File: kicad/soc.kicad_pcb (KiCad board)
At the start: 2 copper layers, 0 parts

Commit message: some kicad stuff
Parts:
- added C1: .001uF, Capacitors_SMD:C_0603_HandSoldering, F.Cu at (78.7, 86.4)
- added J1: JACK_TRS_3PINS, mstock-pretty:SJI-3513N, F.Cu at (134.6, 111.8)
- added J2: PS/2 Keyboard, mstock-pretty:MD-60S, F.Cu at (130.8, 96.5)
- added J3: PS/2 Mouse, mstock-pretty:MD-60S, F.Cu at (130.8, 81.3)
- added P1: LED MATRIX, Pin_Headers:Pin_Header_Straight_2x08, F.Cu at (61.0, 77.5)
- added P10: CODEC right, Socket_Strips:Socket_Strip_Straight_1x16, F.Cu at (148.6, 67.3)
- added P11: CODEC inputs, Pin_Headers:Pin_Header_Straight_1x04, F.Cu at (167.6, 52.1)
- added P2: ALTERA_DE1_GPIO, mstock:PIN_ARRAY_20X2_LARGE, F.Cu at (52.1, 99.1)
- added P3: RTC header, Socket_Strips:Socket_Strip_Straight_1x07, F.Cu at (95.2, 92.7)
- added P6: Amp in, Socket_Strips:Socket_Strip_Straight_1x02, F.Cu at (96.5, 102.9)
- added P7: Amp pwr, Socket_Strips:Socket_Strip_Straight_1x03, F.Cu at (78.7, 116.8)
- added P8: Amp out, Socket_Strips:Socket_Strip_Straight_1x02, F.Cu at (78.7, 102.9)
- added P9: CODEC left, Socket_Strips:Socket_Strip_Straight_1x16, F.Cu at (105.4, 143.5)
- added R1: 10k, Resistors_SMD:R_0603_HandSoldering, F.Cu at (73.7, 86.4)
- added R2: 10k, Resistors_SMD:R_0603_HandSoldering, F.Cu at (83.8, 86.4)
- added R3: 10k, Resistors_SMD:R_0603_HandSoldering, F.Cu at (73.7, 104.1)
- added SP1: SPEAKER, Pin_Headers:Pin_Header_Angled_1x02, F.Cu at (86.4, 77.5)
- added U1: speakjet, Housings_DIP:DIP-18_W7.62mm, F.Cu at (61.0, 87.6)

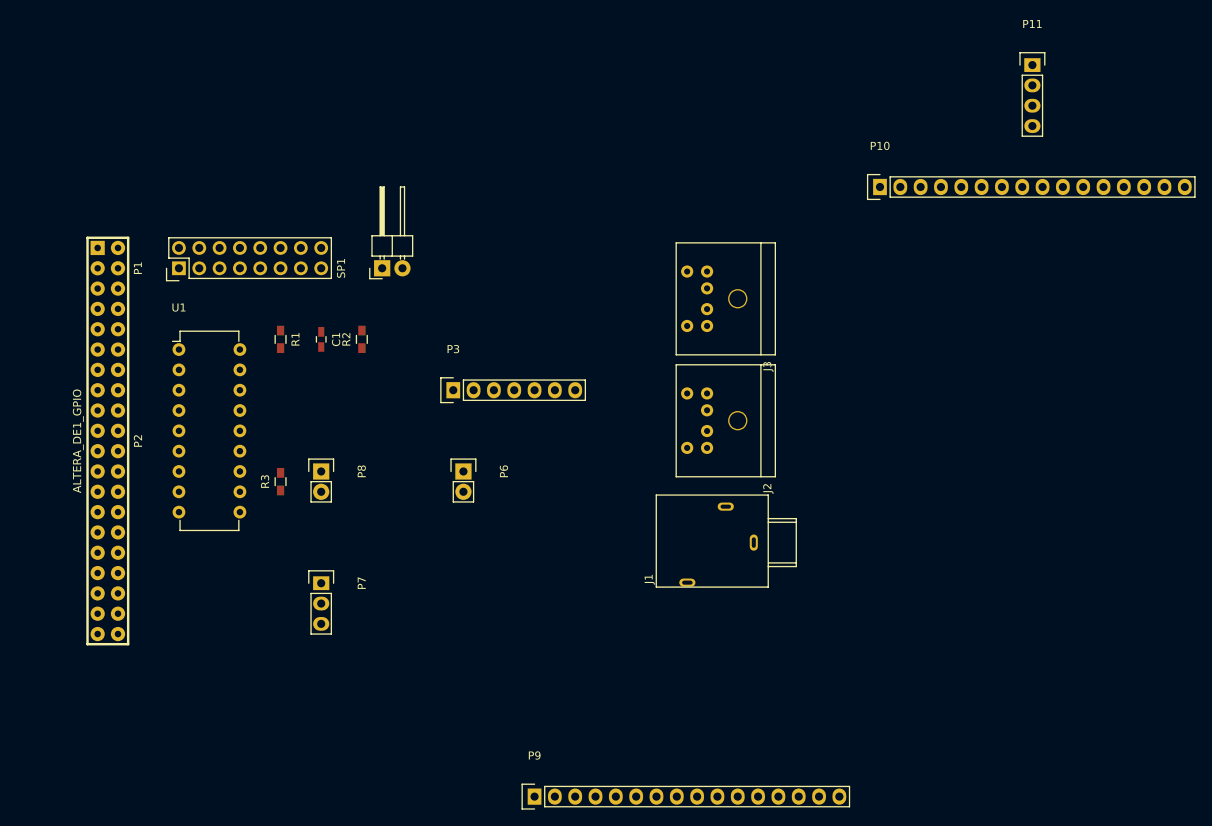
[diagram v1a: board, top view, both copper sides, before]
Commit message: some rework of support board, using the CODEC carrier board, the RTC, and headphone, PS/2 jacks
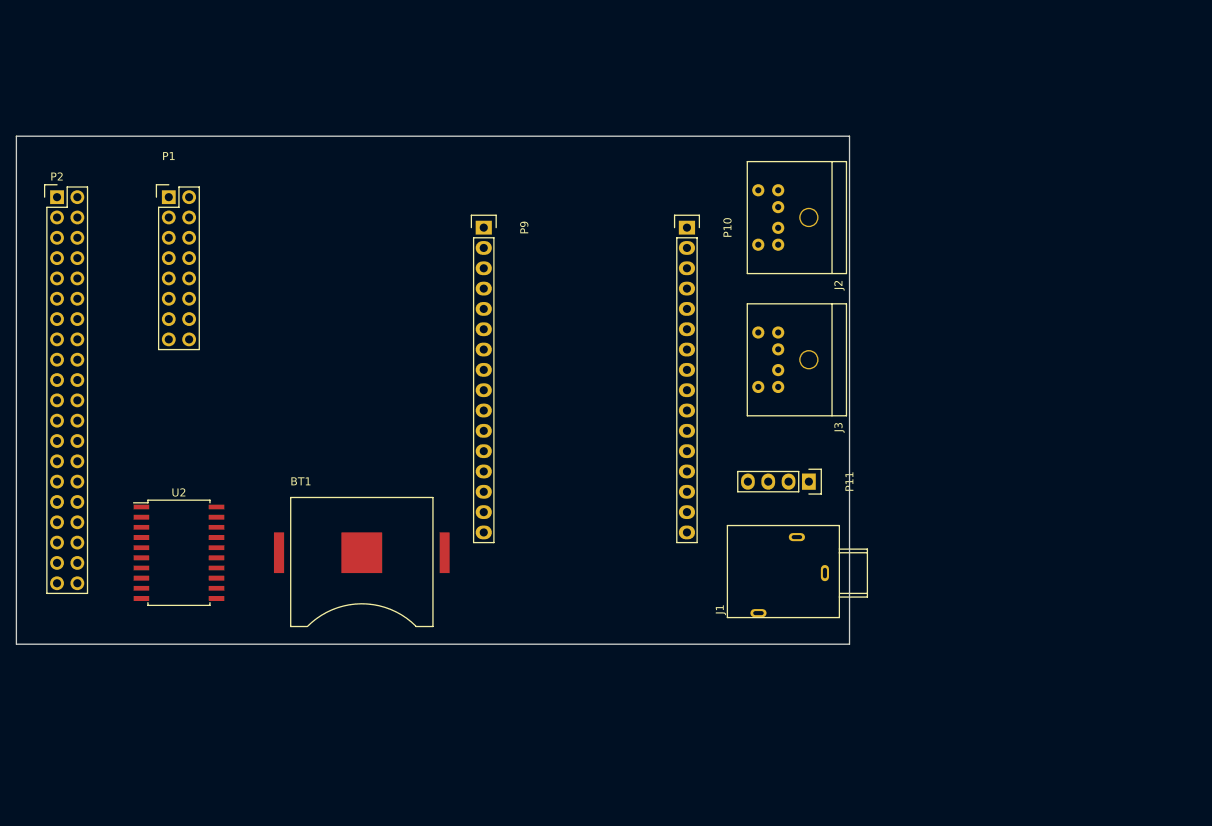
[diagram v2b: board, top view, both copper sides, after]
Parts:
- removed C1: .001uF, Capacitors_SMD:C_0603_HandSoldering
- removed P3: RTC header, Socket_Strips:Socket_Strip_Straight_1x07
- removed P6: Amp in, Socket_Strips:Socket_Strip_Straight_1x02
- removed P7: Amp pwr, Socket_Strips:Socket_Strip_Straight_1x03
- removed P8: Amp out, Socket_Strips:Socket_Strip_Straight_1x02
- removed R1, R2, R3: 10k, Resistors_SMD:R_0603_HandSoldering
- removed SP1: SPEAKER, Pin_Headers:Pin_Header_Angled_1x02
- removed U1: speakjet, Housings_DIP:DIP-18_W7.62mm
- added BT1: 2025 coin cell, mstock-pretty:coincell, F.Cu at (83.8, 113.0)
- added U2: DS3234, Housings_SOIC:SOIC-20_7.5x12.8mm_Pitch1.27mm, F.Cu at (61.0, 113.0)
- P2: footprint mstock:PIN_ARRAY_20X2_LARGE -> Pin_Headers:Pin_Header_Straight_2x20
- moved P9 71.4 mm to (99.1, 72.4), turned to 270 degrees
- moved P11 59.1 mm to (139.7, 104.1), turned to 270 degrees
- moved P2 31.1 mm to (45.7, 68.6), turned to 0 degrees
- moved J2 26.9 mm to (139.7, 71.1)
- moved P10 24.7 mm to (124.5, 72.4), turned to 270 degrees
- moved J3 11.7 mm to (139.7, 88.9)
- moved J1 9.67 mm to (143.5, 115.6)
- moved P1 8.98 mm to (59.7, 68.6), turned to 0 degrees
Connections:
- P2 pad 1: /Serial1 -> (no net)
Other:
- board outline added: 104.1 x 63.5 mm

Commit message: close to final
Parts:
- removed P11: CODEC inputs, Pin_Headers:Pin_Header_Straight_1x04
- added C1: 10nF, Capacitors_SMD:C_0805_HandSoldering, F.Cu at (106.7, 100.3)
- added C2: 10nF, Capacitors_SMD:C_0805_HandSoldering, F.Cu at (106.7, 92.7)
- added C3: 1uF, Capacitors_SMD:C_0805_HandSoldering, F.Cu at (114.3, 100.3)
- added C4: 1uF, Capacitors_SMD:C_0805_HandSoldering, F.Cu at (114.3, 92.7)
- added J4: Line In, mstock-pretty:SJI-3513N, F.Cu at (143.5, 102.9)
- added P3: Bluetooth, Socket_Strips:Socket_Strip_Straight_1x09, F.Cu at (71.1, 85.1)
- added P4: CONN_01X08, Pin_Headers:Pin_Header_Straight_2x04, F.Cu at (57.1, 92.7)
- added R1: 470, Resistors_SMD:R_0805_HandSoldering, F.Cu at (114.3, 106.7)
- added R2: 470, Resistors_SMD:R_0805_HandSoldering, F.Cu at (114.3, 86.4)
- J1: value JACK_TRS_3PINS -> Line Out
- moved P1 3.59 mm to (57.1, 66.0)
- moved BT1 2.54 mm to (81.3, 113.0)
- moved J1 1.27 mm to (143.5, 116.8)
- moved J2 1.27 mm to (139.7, 69.8)
- moved J3 1.27 mm to (139.7, 87.6)
- moved U2 1.27 mm to (59.7, 113.0)
- moved P10 1.27 mm to (123.2, 72.4)
- moved P9 1.27 mm to (100.3, 72.4)
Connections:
- net Net-(J1-Pad2) renamed /L_OUT
- net Net-(J1-Pad3) renamed /R_OUT
- J1 pad 1: Net-(J1-Pad1) -> GNDA
- J2 pad 2: (no net) -> Net-(J2-Pad2)
- J2 pad 6: (no net) -> Net-(J2-Pad6)
- J3 pad 2: (no net) -> Net-(J3-Pad2)
- J3 pad 6: (no net) -> Net-(J3-Pad6)
- P1 pad 12: (no net) -> Net-(P1-Pad12)
- P10 pad 1: (no net) -> Net-(P10-Pad1)
- P10 pad 10: (no net) -> Net-(P10-Pad10)
- P10 pad 11: (no net) -> Net-(P10-Pad11)
- P10 pad 12: (no net) -> Net-(P10-Pad12)
- P10 pad 13: Net-(P10-Pad13) -> GNDA
- P10 pad 15: Net-(P10-Pad15) -> /L_IN
- P10 pad 16: Net-(P10-Pad16) -> /R_IN
- P10 pad 2: (no net) -> Net-(P10-Pad2)
- P10 pad 3: (no net) -> Net-(P10-Pad3)
- P10 pad 4: (no net) -> Net-(P10-Pad4)
- P10 pad 5: (no net) -> Net-(P10-Pad5)
- P10 pad 6: (no net) -> Net-(P10-Pad6)
- P10 pad 7: (no net) -> Net-(P10-Pad7)
- P10 pad 8: (no net) -> Net-(P10-Pad8)
- P10 pad 9: (no net) -> Net-(P10-Pad9)
- P2 pad 1: (no net) -> /Serial1
- P2 pad 20: (no net) -> /IO_17
- P2 pad 21: (no net) -> /~BLE_CS
- P2 pad 22: (no net) -> /IO_19
- P2 pad 23: (no net) -> /IO_20
- P2 pad 24: (no net) -> /BLE_IRQ
- P2 pad 35: (no net) -> /IO_30
- P2 pad 36: (no net) -> /IO_31
- P2 pad 37: (no net) -> /IO_32
- P9 pad 13: Net-(J1-Pad1) -> GNDA
- P9 pad 14: Net-(J1-Pad1) -> GNDA
- P9 pad 2: (no net) -> Net-(P9-Pad2)
- P9 pad 9: (no net) -> Net-(P9-Pad9)
- U2 pad 10: (no net) -> Net-(U2-Pad10)
- U2 pad 11: (no net) -> Net-(U2-Pad11)
- U2 pad 12: (no net) -> Net-(U2-Pad12)
- U2 pad 13: (no net) -> Net-(U2-Pad13)
- U2 pad 14: (no net) -> Net-(U2-Pad14)
- U2 pad 2: (no net) -> Net-(U2-Pad2)
- U2 pad 3: (no net) -> Net-(U2-Pad3)
- U2 pad 5: (no net) -> Net-(U2-Pad5)
- U2 pad 6: (no net) -> Net-(U2-Pad6)
- U2 pad 7: (no net) -> Net-(U2-Pad7)
- U2 pad 8: (no net) -> Net-(U2-Pad8)
- U2 pad 9: (no net) -> Net-(U2-Pad9)
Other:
- board text added: "Bexkat Systems LLC 2016 www.bexkat.com"
- board text added: "DE1 I/O Board v1.0"

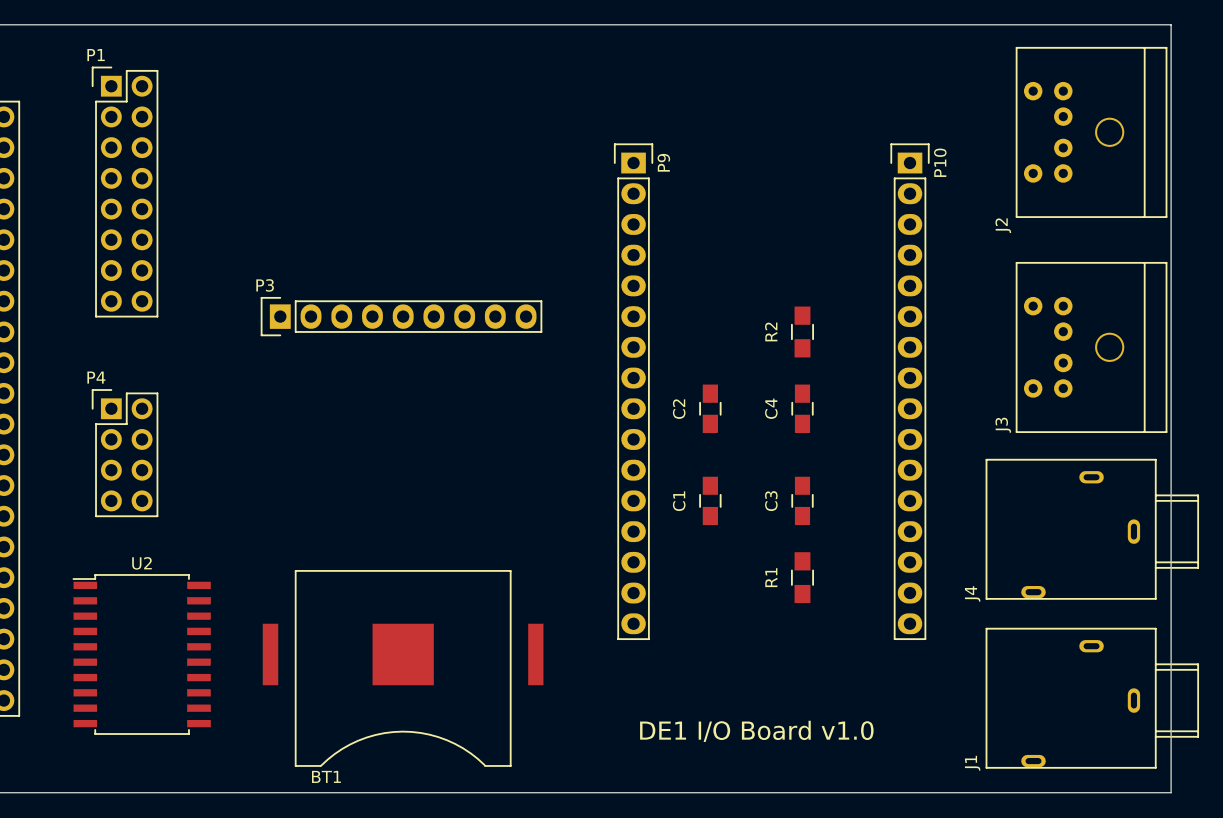
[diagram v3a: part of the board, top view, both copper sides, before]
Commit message: Revert "close to final"
This reverts commit c876cf625f705db1e319b0381db18ed40929d998.
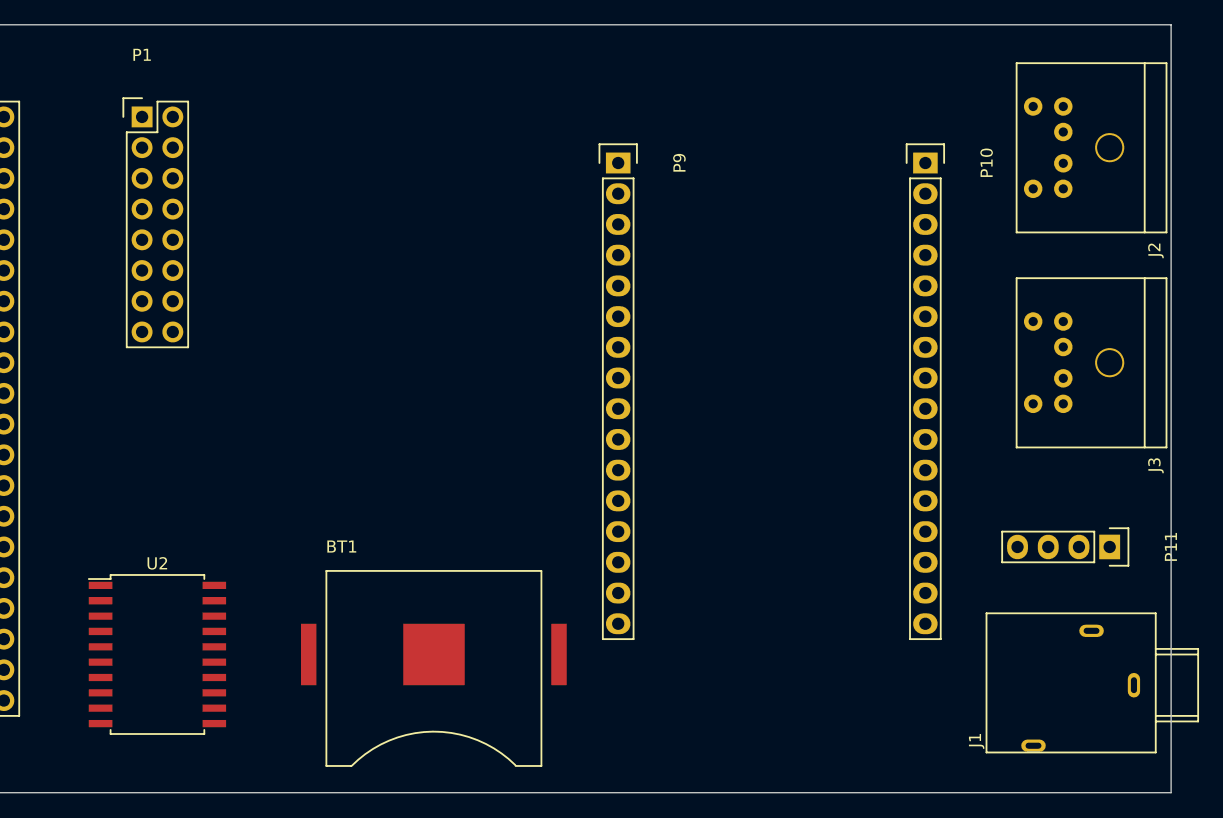
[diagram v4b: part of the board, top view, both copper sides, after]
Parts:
- removed C1, C2: 10nF, Capacitors_SMD:C_0805_HandSoldering
- removed C3, C4: 1uF, Capacitors_SMD:C_0805_HandSoldering
- removed J4: Line In, mstock-pretty:SJI-3513N
- removed P3: Bluetooth, Socket_Strips:Socket_Strip_Straight_1x09
- removed P4: CONN_01X08, Pin_Headers:Pin_Header_Straight_2x04
- removed R1, R2: 470, Resistors_SMD:R_0805_HandSoldering
- added P11: CODEC inputs, Pin_Headers:Pin_Header_Straight_1x04, F.Cu at (139.7, 104.1)
- J1: value Line Out -> JACK_TRS_3PINS
- moved P1 3.59 mm to (59.7, 68.6)
- moved BT1 2.54 mm to (83.8, 113.0)
- moved J1 1.27 mm to (143.5, 115.6)
- moved J2 1.27 mm to (139.7, 71.1)
- moved J3 1.27 mm to (139.7, 88.9)
- moved U2 1.27 mm to (61.0, 113.0)
- moved P10 1.27 mm to (124.5, 72.4)
- moved P9 1.27 mm to (99.1, 72.4)
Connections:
- net /L_OUT renamed Net-(J1-Pad2)
- net /R_OUT renamed Net-(J1-Pad3)
- J1 pad 1: GNDA -> Net-(J1-Pad1)
- J2 pad 2: Net-(J2-Pad2) -> (no net)
- J2 pad 6: Net-(J2-Pad6) -> (no net)
- J3 pad 2: Net-(J3-Pad2) -> (no net)
- J3 pad 6: Net-(J3-Pad6) -> (no net)
- P1 pad 12: Net-(P1-Pad12) -> (no net)
- P10 pad 1: Net-(P10-Pad1) -> (no net)
- P10 pad 10: Net-(P10-Pad10) -> (no net)
- P10 pad 11: Net-(P10-Pad11) -> (no net)
- P10 pad 12: Net-(P10-Pad12) -> (no net)
- P10 pad 13: GNDA -> Net-(P10-Pad13)
- P10 pad 15: /L_IN -> Net-(P10-Pad15)
- P10 pad 16: /R_IN -> Net-(P10-Pad16)
- P10 pad 2: Net-(P10-Pad2) -> (no net)
- P10 pad 3: Net-(P10-Pad3) -> (no net)
- P10 pad 4: Net-(P10-Pad4) -> (no net)
- P10 pad 5: Net-(P10-Pad5) -> (no net)
- P10 pad 6: Net-(P10-Pad6) -> (no net)
- P10 pad 7: Net-(P10-Pad7) -> (no net)
- P10 pad 8: Net-(P10-Pad8) -> (no net)
- P10 pad 9: Net-(P10-Pad9) -> (no net)
- P2 pad 1: /Serial1 -> (no net)
- P2 pad 20: /IO_17 -> (no net)
- P2 pad 21: /~BLE_CS -> (no net)
- P2 pad 22: /IO_19 -> (no net)
- P2 pad 23: /IO_20 -> (no net)
- P2 pad 24: /BLE_IRQ -> (no net)
- P2 pad 35: /IO_30 -> (no net)
- P2 pad 36: /IO_31 -> (no net)
- P2 pad 37: /IO_32 -> (no net)
- P9 pad 13: GNDA -> Net-(J1-Pad1)
- P9 pad 14: GNDA -> Net-(J1-Pad1)
- P9 pad 2: Net-(P9-Pad2) -> (no net)
- P9 pad 9: Net-(P9-Pad9) -> (no net)
- U2 pad 10: Net-(U2-Pad10) -> (no net)
- U2 pad 11: Net-(U2-Pad11) -> (no net)
- U2 pad 12: Net-(U2-Pad12) -> (no net)
- U2 pad 13: Net-(U2-Pad13) -> (no net)
- U2 pad 14: Net-(U2-Pad14) -> (no net)
- U2 pad 2: Net-(U2-Pad2) -> (no net)
- U2 pad 3: Net-(U2-Pad3) -> (no net)
- U2 pad 5: Net-(U2-Pad5) -> (no net)
- U2 pad 6: Net-(U2-Pad6) -> (no net)
- U2 pad 7: Net-(U2-Pad7) -> (no net)
- U2 pad 8: Net-(U2-Pad8) -> (no net)
- U2 pad 9: Net-(U2-Pad9) -> (no net)
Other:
- board text removed: "Bexkat Systems LLC 2016 www.bexkat.com"
- board text removed: "DE1 I/O Board v1.0"
